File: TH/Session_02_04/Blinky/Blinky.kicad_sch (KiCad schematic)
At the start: 12 parts, among them SW1 SW_SPDT, U1 TLC551CD‎

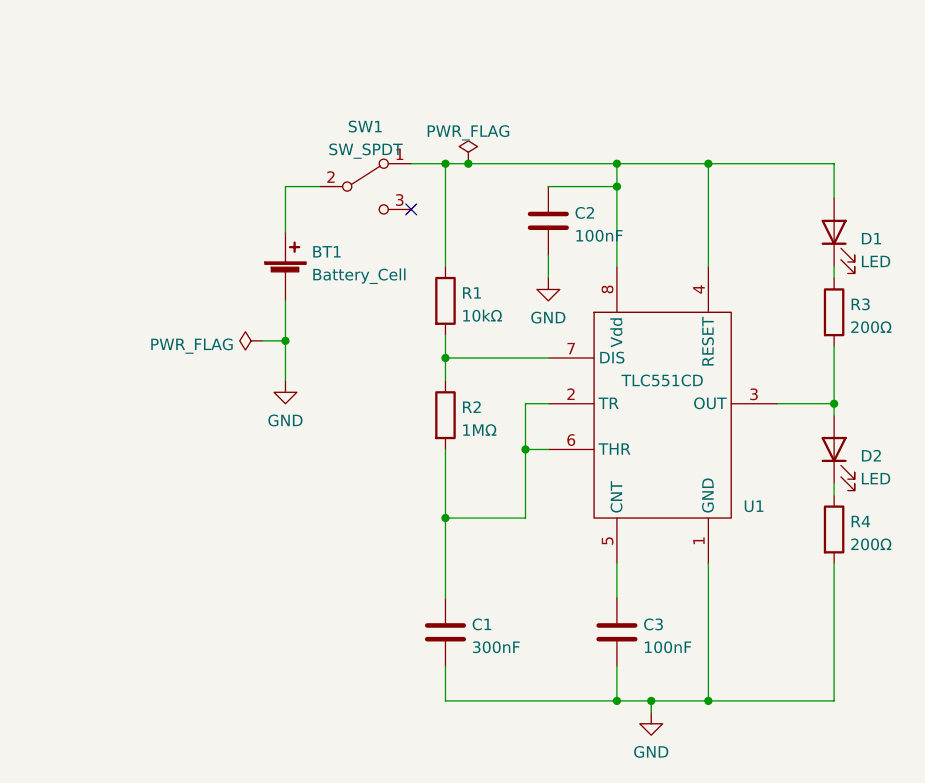
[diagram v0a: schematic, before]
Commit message: Revamps the through-hole project as transistor based
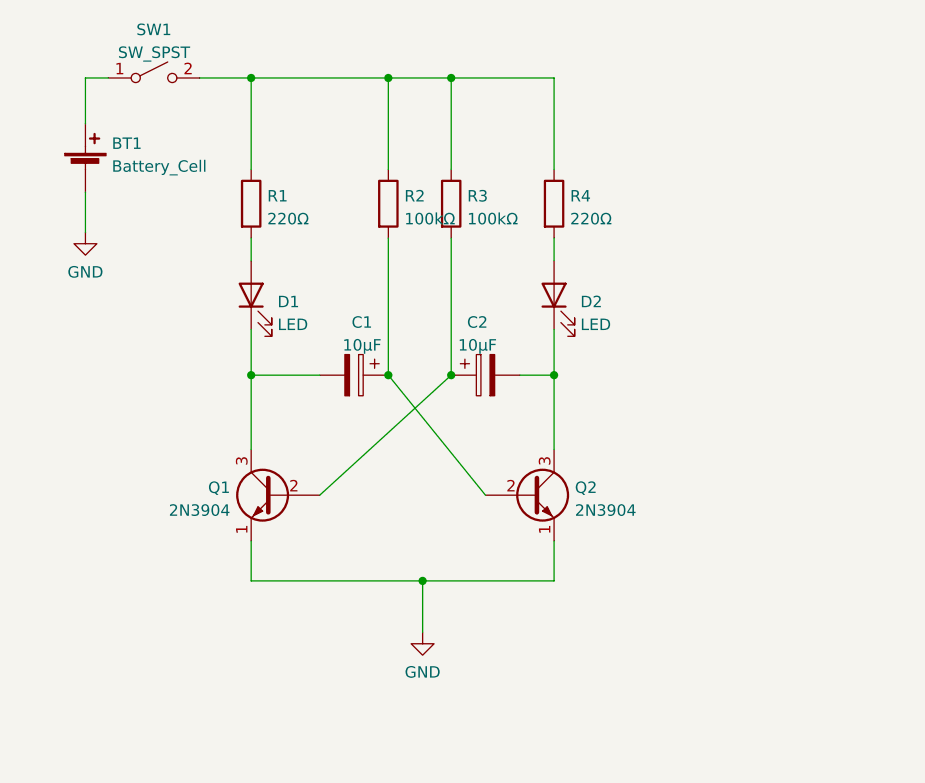
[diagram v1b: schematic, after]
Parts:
- removed C1: 300nF, Capacitor_THT:C_Disc_D5.0mm_W2.5mm_P5.00mm, symbol Device:C
- removed C2, C3: 100nF, Capacitor_THT:C_Disc_D5.0mm_W2.5mm_P5.00mm, symbol Device:C
- removed SW1: SW_SPDT, Blinky_ZAM:SSK-1202, symbol Switch:SW_SPDT
- removed U1: TLC551CD‎, Package_DIP:DIP-8_W7.62mm_Socket, symbol Blinky:TLC551CD‎
- added C1, C2: 10μF, Capacitor_THT:CP_Radial_D5.0mm_P2.50mm, symbol Device:C_Polarized
- added Q1, Q2: 2N3904, Package_TO_SOT_THT:TO-92_Inline, symbol Transistor_BJT:2N3904
- added SW1: SW_SPST, Blinky_ZAM:SSK-1202, symbol Switch:SW_SPST
- R1: value 10kΩ -> 220Ω; footprint Resistor_THT:R_Axial_DIN0207_L6.3mm_D2.5mm_P10.16mm_Horizontal -> Resistor_THT:R_Axial_DIN0207_L6.3mm_D2.5mm_P2.54mm_Vertical
- R2: value 1MΩ -> 100kΩ; footprint Resistor_THT:R_Axial_DIN0207_L6.3mm_D2.5mm_P10.16mm_Horizontal -> Resistor_THT:R_Axial_DIN0207_L6.3mm_D2.5mm_P2.54mm_Vertical
- R3: value 200Ω -> 100kΩ; footprint Resistor_THT:R_Axial_DIN0207_L6.3mm_D2.5mm_P10.16mm_Horizontal -> Resistor_THT:R_Axial_DIN0207_L6.3mm_D2.5mm_P2.54mm_Vertical
- R4: value 200Ω -> 220Ω; footprint Resistor_THT:R_Axial_DIN0207_L6.3mm_D2.5mm_P10.16mm_Horizontal -> Resistor_THT:R_Axial_DIN0207_L6.3mm_D2.5mm_P2.54mm_Vertical
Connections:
- net GND: now also Q1.1 (E), Q2.1 (E); no longer R4.2
- net at R2.2: now also C1.1, Q2.2 (B)
- net at R3.2: now also C2.1, Q1.2 (B); no longer D2.2 (A)
- net at R1.1: now also R2.1, R3.1, R4.1, SW1.2 (B); no longer D1.2 (A)
- net at R1.2: now also D1.2 (A); no longer R2.1
- net at D2.1 (K): now also C2.2, Q2.3 (C); no longer R4.1
- net at D1.1 (K): now also C1.2, Q1.3 (C); no longer R3.1
- net at BT1.1 (+): now also SW1.1 (A)
- new net: D2.2 (A), R4.2
- no-connect marks 1 -> 0

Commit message: Makes corrections to the design rules
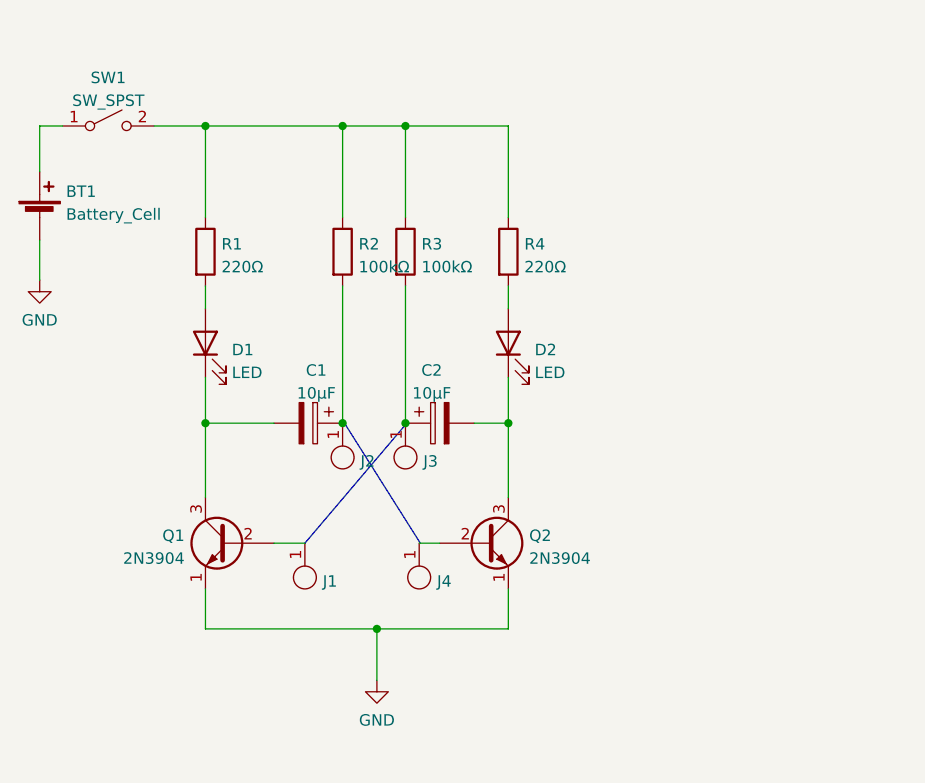
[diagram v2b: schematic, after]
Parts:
- added J1, J2, J3, J4: Jumper_1, TestPoint:TestPoint_THTPad_2.0x2.0mm_Drill1.0mm, symbol Blinky:Jumper_1
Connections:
- net at C2.1, R3.2: now also J3.1; no longer Q1.2 (B)
- net at C1.1, R2.2: now also J2.1; no longer Q2.2 (B)
- new net: J4.1, Q2.2 (B)
- new net: J1.1, Q1.2 (B)
